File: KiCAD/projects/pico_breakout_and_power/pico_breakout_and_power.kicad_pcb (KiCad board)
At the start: 2 copper layers, 40.9 x 64.3 mm, 12 parts, among them IC1 STCS05DR, J1 Conn_01x05_Socket

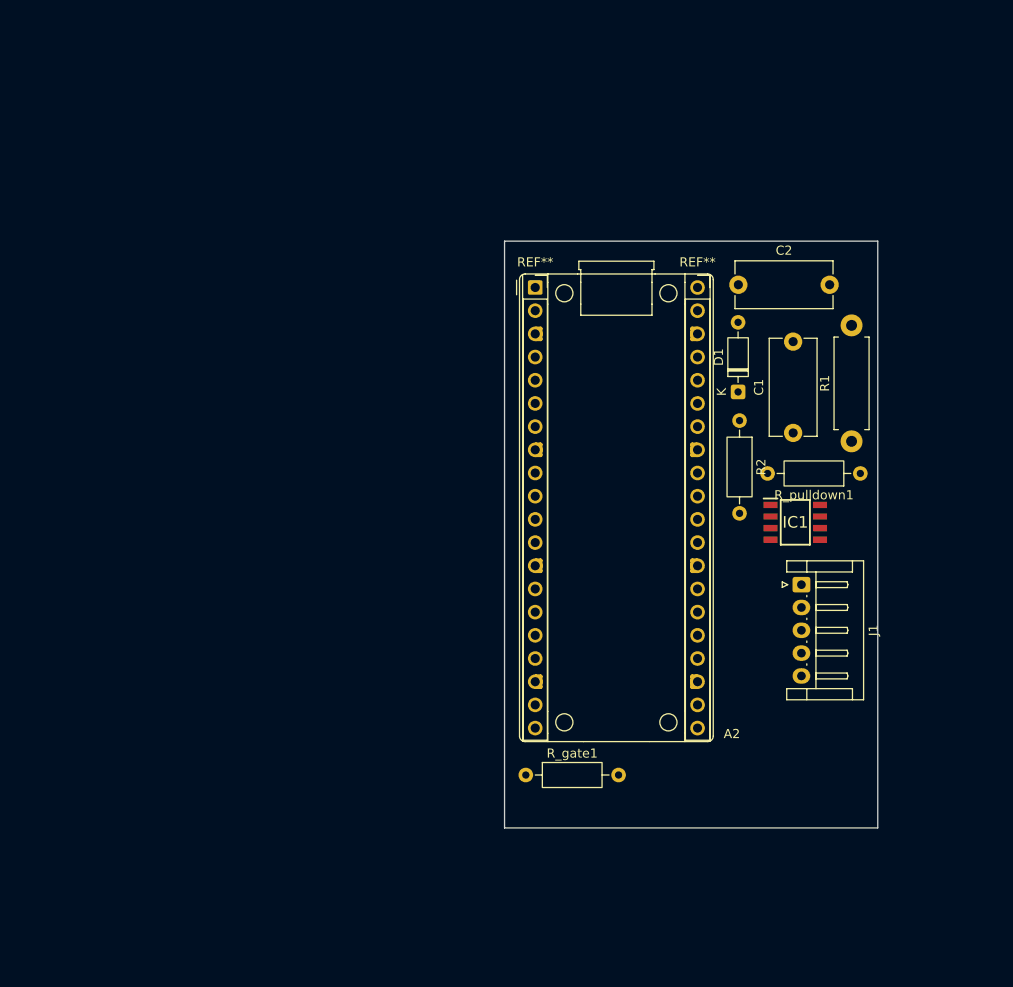
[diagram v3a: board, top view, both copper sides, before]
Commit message: Routed combined pico board
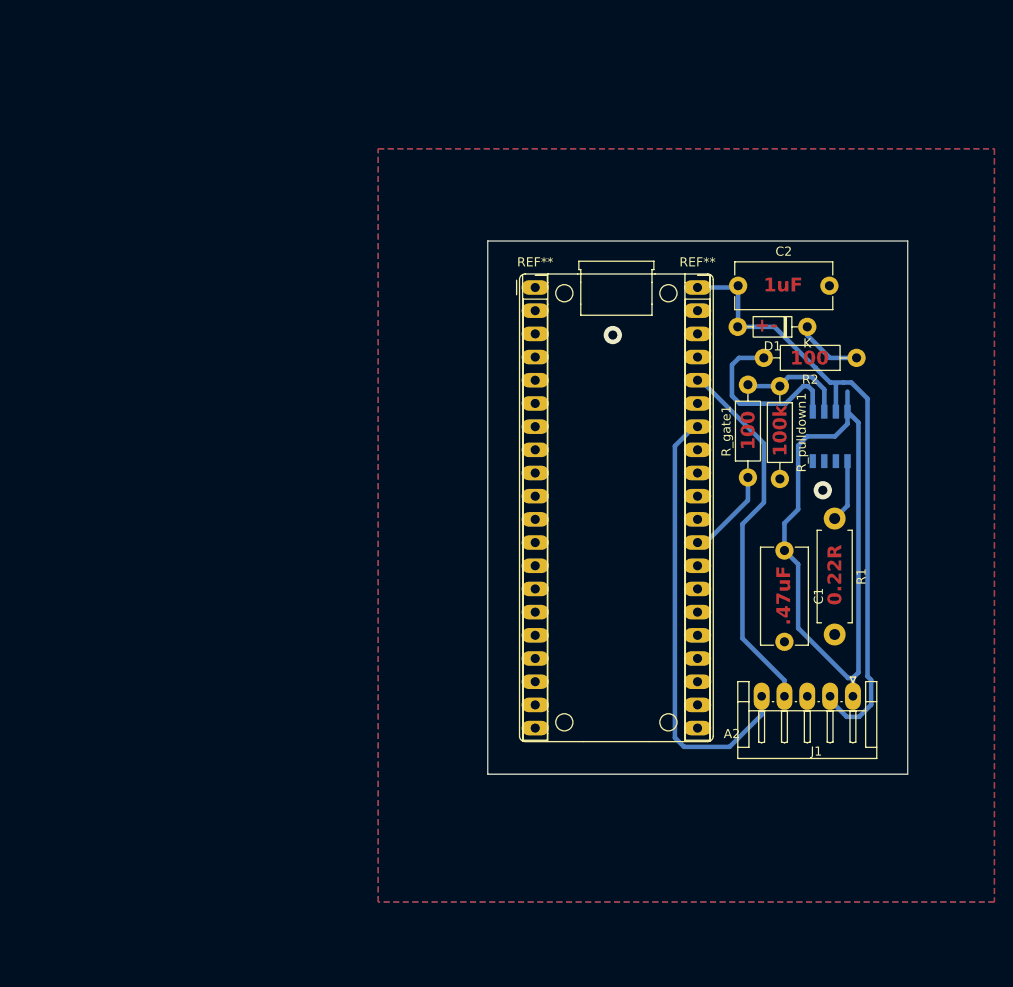
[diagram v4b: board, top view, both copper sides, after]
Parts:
- IC1: moved to B.Cu
- moved R_gate1 40.7 mm to (150.5, 78.5), turned to 90 degrees
- moved R2 14.5 mm to (162.4, 65.4), turned to 180 degrees
- moved J1 13.5 mm to (162.0, 102.5), turned to 180 degrees
- moved R_pulldown1 13.0 mm to (154.0, 68.5), turned to -90 degrees
- moved C1 12.9 mm to (154.5, 86.5), turned to -90 degrees
- moved D1 10.4 mm to (157.0, 62.0), turned to 180 degrees
- moved IC1 10.2 mm to (159.5, 74.0), turned to -90 degrees
- moved R1 8.66 mm to (160.0, 83.0), turned to -90 degrees
- moved C2 0.11 mm to (149.4, 57.5)
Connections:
- A2 pad 40: /Anode -> /VBUS_5V/ANODE
- C2 pad 1: /Anode -> /VBUS_5V/ANODE
- D1 pad 2: /Anode -> /VBUS_5V/ANODE
- IC1 pad 3: /Anode -> /VBUS_5V/ANODE
- J1 pad 1: /3V3(OUT) -> /Cathode
- J1 pad 2: /GPIO28_ADC2 -> /VBUS_5V/ANODE
- J1 pad 4: /Anode -> /3V3(OUT)
- J1 pad 5: /Cathode -> /GPIO28_ADC2
- R_gate1 pad 1: /GPIO15 -> /GPIO22
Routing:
- net /Cathode: track 0.00 -> 71.4 mm
- net /VBUS_5V/ANODE: track 0.00 -> 69.8 mm
- net /GPIO28_ADC2: track 0.00 -> 48.7 mm
- net /3V3(OUT): track 0.00 -> 40.7 mm
- net Net-(IC1-VCC): track 0.00 -> 19.7 mm
- net Net-(IC1-PWM): track 0.00 -> 11.9 mm
- net /GPIO22: track 0.00 -> 9.94 mm
- net Net-(D1-K): track 0.00 -> 7.35 mm
- net Net-(IC1-FB): track 0.00 -> 6.87 mm
- net GND: vias 0 -> 2
- added copper zone on B.Cu, net GND
- added copper zone on F.Cu, net GND
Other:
- board size 40.9 x 64.3 mm -> 46 x 58.4 mm
- board text added: "+-"
- board text added: ".47uF"
- board text added: "0.22R"
- board text added: "100"
- board text added: "100k"
- board text added: "1uF"

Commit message: First version of pico breakout submitted for manufacturing. Thicker traces and pads
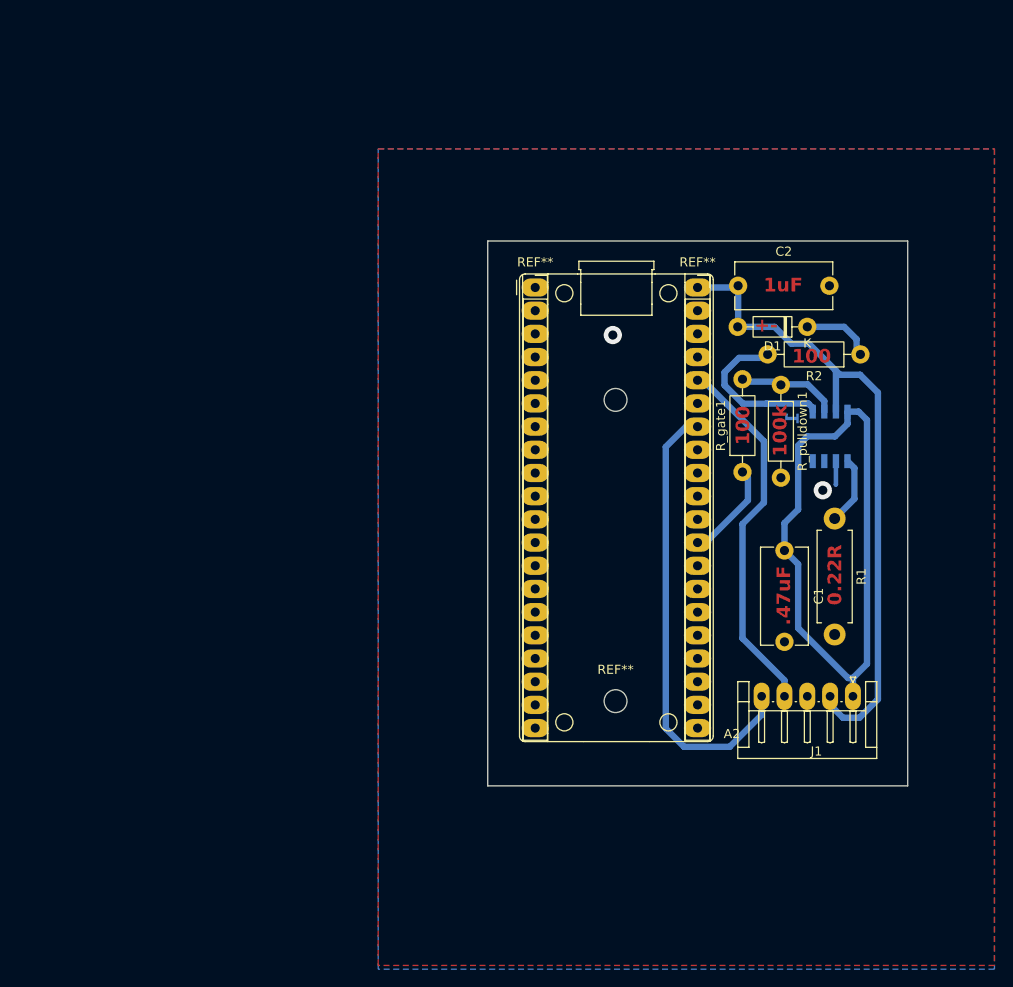
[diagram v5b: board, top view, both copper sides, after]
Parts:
- added ?: , , F.Cu at (136.0, 70.0)
- added REF**: MountingHole_2.5mm, MountingHole:MountingHole_2.5mm, F.Cu at (136.0, 103.0)
- moved R_gate1 0.85 mm to (149.9, 77.9)
- moved R2 0.57 mm to (162.8, 65.0)
- moved R_pulldown1 0.18 mm to (154.1, 68.4)
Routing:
- net /VBUS_5V/ANODE: track 69.8 -> 73.3 mm
- net GND: track 0.00 -> 2.57 mm
- net Net-(IC1-VCC): track 19.7 -> 18.1 mm
- net /GPIO28_ADC2: track 48.7 -> 50.1 mm
- net /GPIO22: track 9.94 -> 10.8 mm
- net /Cathode: track 71.4 -> 70.7 mm
- net Net-(IC1-PWM): track 11.9 -> 11.2 mm
- net Net-(IC1-FB): track 6.87 -> 7.50 mm
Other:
- board size 46 x 58.4 mm -> 46 x 59.7 mm
- board text added: "1"

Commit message: Final Pico breakout board.
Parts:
- removed ?: , 
- removed the REF** at (136.0, 103.0)
- moved R_gate1 0.85 mm to (150.5, 78.5)
- moved R2 0.57 mm to (162.4, 65.4)
- moved R_pulldown1 0.18 mm to (154.0, 68.5)
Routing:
- net /VBUS_5V/ANODE: track 73.3 -> 69.8 mm
- net GND: track 2.57 -> 0.00 mm
- net Net-(IC1-VCC): track 18.1 -> 19.7 mm
- net /GPIO28_ADC2: track 50.1 -> 48.7 mm
- net /GPIO22: track 10.8 -> 9.94 mm
- net /Cathode: track 70.7 -> 71.4 mm
- net Net-(IC1-PWM): track 11.2 -> 11.9 mm
- net Net-(IC1-FB): track 7.50 -> 6.87 mm
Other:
- board size 46 x 59.7 mm -> 46 x 58.4 mm
- board text removed: "1"
